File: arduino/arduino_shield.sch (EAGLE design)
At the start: 19 parts, among them IC3 PCF8574T, IC4 PCF8574T

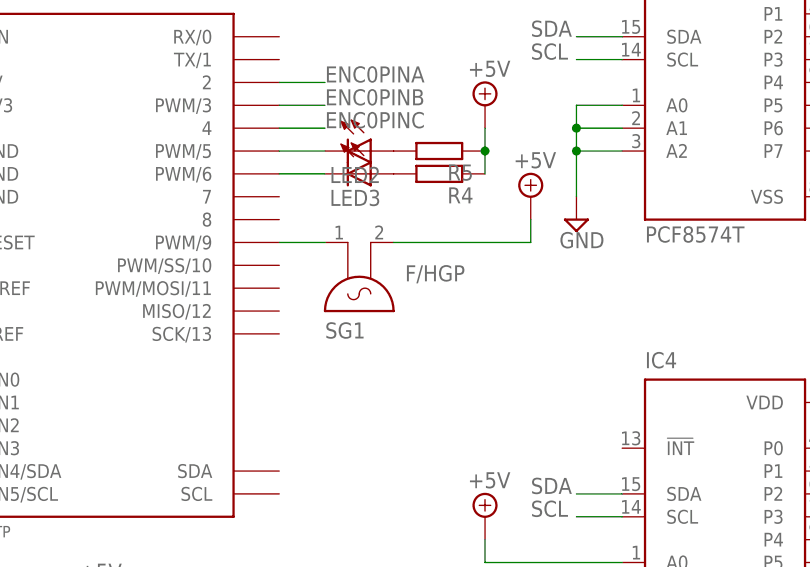
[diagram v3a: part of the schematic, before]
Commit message: Pinheader auf 2.5, Summer gändert, Beschriftung
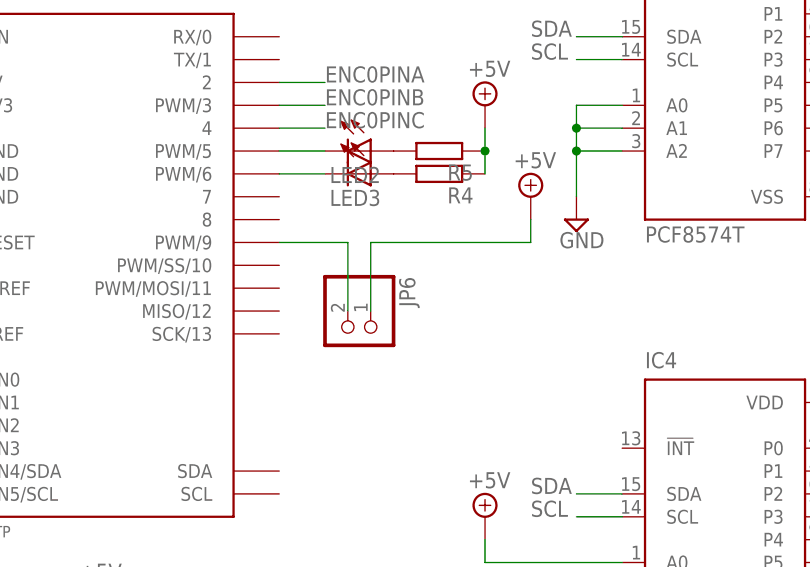
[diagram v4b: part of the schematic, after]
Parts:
- removed SG1: F/HGP, buzzer:F/HGP
- added JP6: (no value), pinhead:PINHD-1X2
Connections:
- net +5V: now also JP6.1; no longer SG1.2
- net N$34: now also JP6.2; no longer SG1.1
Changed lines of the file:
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@@
 <part name="JP4" library="pinheader_250" deviceset="PINHD-1X10" device=""/>
 <part name="SUPPLY16" library="supply2" deviceset="+5V" device=""/>
-<part name="SG1" library="buzzer" deviceset="F/HGP" device=""/>
 <part name="SUPPLY21" library="supply2" deviceset="+5V" device=""/>
 <part name="SUPPLY13" library="supply2" deviceset="+15V" device="" value="+16V"/>
@@
 <part name="SUPPLY26" library="supply2" deviceset="+5V" device=""/>
 <part name="FRAME1" library="frames" deviceset="A4L-LOC" device=""/>
+<part name="JP6" library="pinhead" deviceset="PINHD-1X2" device=""/>
 </parts>
 <sheets>
@@
 <instance part="JP4" gate="A" x="78.74" y="50.8"/>
 <instance part="SUPPLY16" gate="+5V" x="35.56" y="-48.26"/>
-<instance part="SG1" gate="G$1" x="-50.8" y="25.4" rot="MR180"/>
 <instance part="SUPPLY21" gate="+5V" x="-30.48" y="33.02"/>
 <instance part="SUPPLY13" gate="+15V" x="-99.06" y="-33.02"/>
@@
 <instance part="SUPPLY26" gate="+5V" x="-35.56" y="43.18"/>
 <instance part="FRAME1" gate="G$1" x="-142.24" y="-96.52"/>
+<instance part="JP6" gate="G$1" x="-50.8" y="17.78" rot="R270"/>
 </instances>
 <busses>
@@
 </segment>
 <segment>
-<pinref part="SG1" gate="G$1" pin="2"/>
-<wire x1="-45.72" y1="27.94" x2="-30.48" y2="27.94" width="0.1524" layer="91"/>
+<wire x1="-48.26" y1="27.94" x2="-30.48" y2="27.94" width="0.1524" layer="91"/>
 <wire x1="-30.48" y1="27.94" x2="-30.48" y2="30.48" width="0.1524" layer="91"/>
 <pinref part="SUPPLY21" gate="+5V" pin="+5V"/>
+<pinref part="JP6" gate="G$1" pin="1"/>
+<wire x1="-48.26" y1="27.94" x2="-48.26" y2="20.32" width="0.1524" layer="91"/>
 </segment>
 <segment>
@@
 <segment>
 <pinref part="ARD1" gate="G$1" pin="PWM/9"/>
-<pinref part="SG1" gate="G$1" pin="1"/>
-<wire x1="-58.42" y1="27.94" x2="-53.34" y2="27.94" width="0.1524" layer="91"/>
-</segment>
-</net>
+<wire x1="-58.42" y1="27.94" x2="-50.8" y2="27.94" width="0.1524" layer="91"/>
+<pinref part="JP6" gate="G$1" pin="2"/>
+<wire x1="-50.8" y1="27.94" x2="-50.8" y2="20.32" width="0.1524" layer="91"/>
+</segment>
+</net>

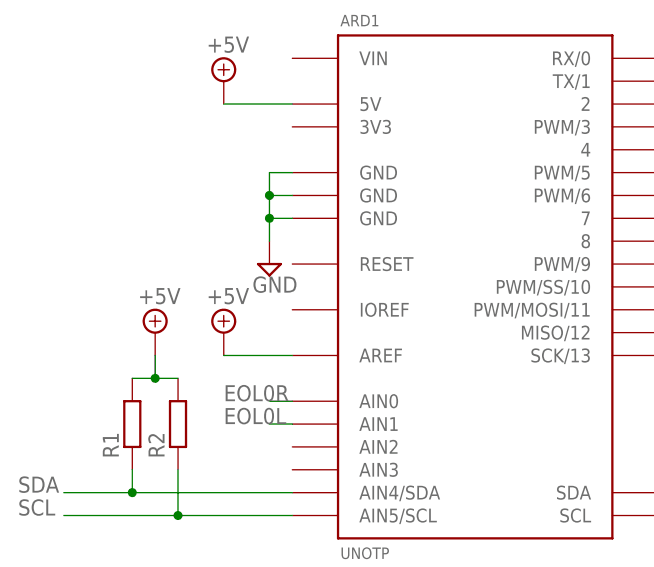
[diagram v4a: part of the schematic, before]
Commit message: Qt Project entfernt
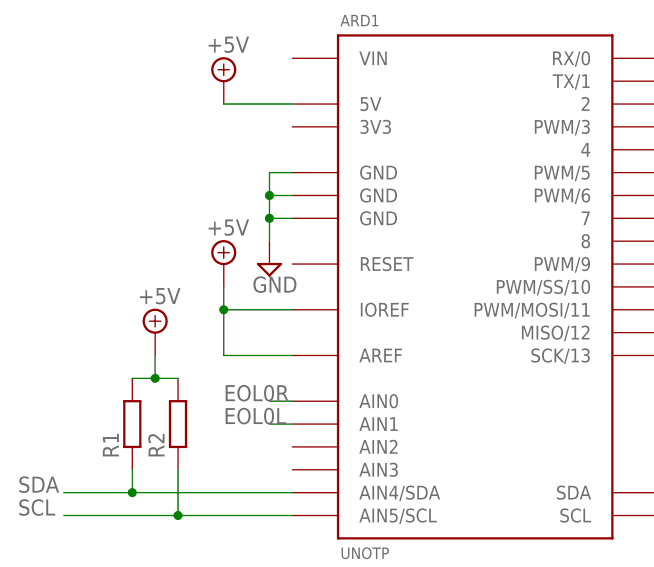
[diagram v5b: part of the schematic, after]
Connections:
- net +5V: now also ARD1.IOREF
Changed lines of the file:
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@@
 <instance part="SUPPLY12" gate="GND" x="-30.48" y="-63.5"/>
 <instance part="SUPPLY19" gate="GND" x="-17.78" y="-68.58"/>
-<instance part="SUPPLY20" gate="+5V" x="-106.68" y="20.32"/>
+<instance part="SUPPLY20" gate="+5V" x="-106.68" y="27.94"/>
 <instance part="SUPPLY15" gate="G$1" x="-119.38" y="-33.02"/>
 <instance part="SUPPLY22" gate="+5V" x="-78.74" y="-12.7"/>
@@
 </segment>
 <segment>
-<pinref part="ARD1" gate="G$1" pin="AREF"/>
-<pinref part="SUPPLY20" gate="+5V" pin="+5V"/>
-<wire x1="-99.06" y1="17.78" x2="-106.68" y2="17.78" width="0.1524" layer="91"/>
-</segment>
-<segment>
 <pinref part="SUPPLY22" gate="+5V" pin="+5V"/>
 <pinref part="R3" gate="G$1" pin="2"/>
@@
 <junction x="-35.56" y="38.1"/>
 </segment>
+<segment>
+<pinref part="ARD1" gate="G$1" pin="IOREF"/>
+<pinref part="SUPPLY20" gate="+5V" pin="+5V"/>
+<wire x1="-99.06" y1="22.86" x2="-106.68" y2="22.86" width="0.1524" layer="91"/>
+<wire x1="-106.68" y1="22.86" x2="-106.68" y2="25.4" width="0.1524" layer="91"/>
+<pinref part="ARD1" gate="G$1" pin="AREF"/>
+<wire x1="-99.06" y1="17.78" x2="-106.68" y2="17.78" width="0.1524" layer="91"/>
+<wire x1="-106.68" y1="17.78" x2="-106.68" y2="22.86" width="0.1524" layer="91"/>
+<junction x="-106.68" y="22.86"/>
+</segment>
 </net>
